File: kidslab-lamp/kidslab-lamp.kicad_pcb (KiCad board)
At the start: 2 copper layers, 129.2 x 177.1 mm, 2 parts, among them U1 Pico

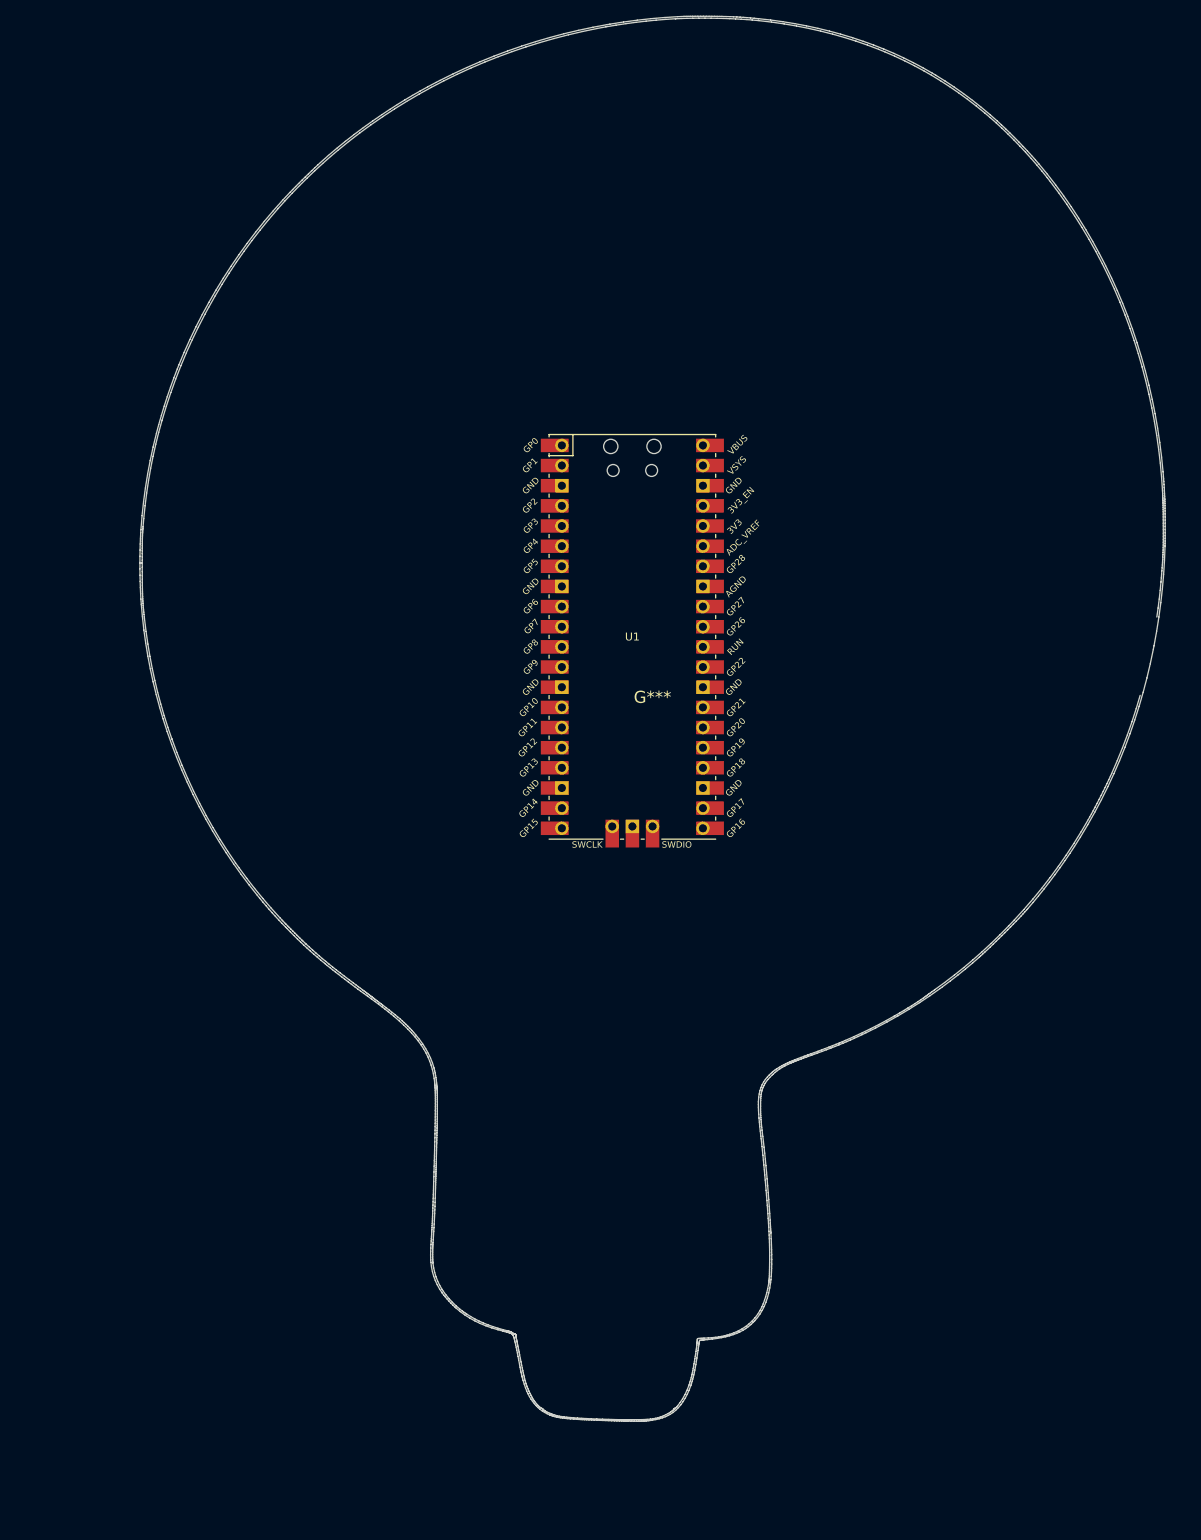
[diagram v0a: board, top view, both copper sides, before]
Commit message: new pcb outline, added frisbee footprints, smaller PCB, added arrow footprints etc.
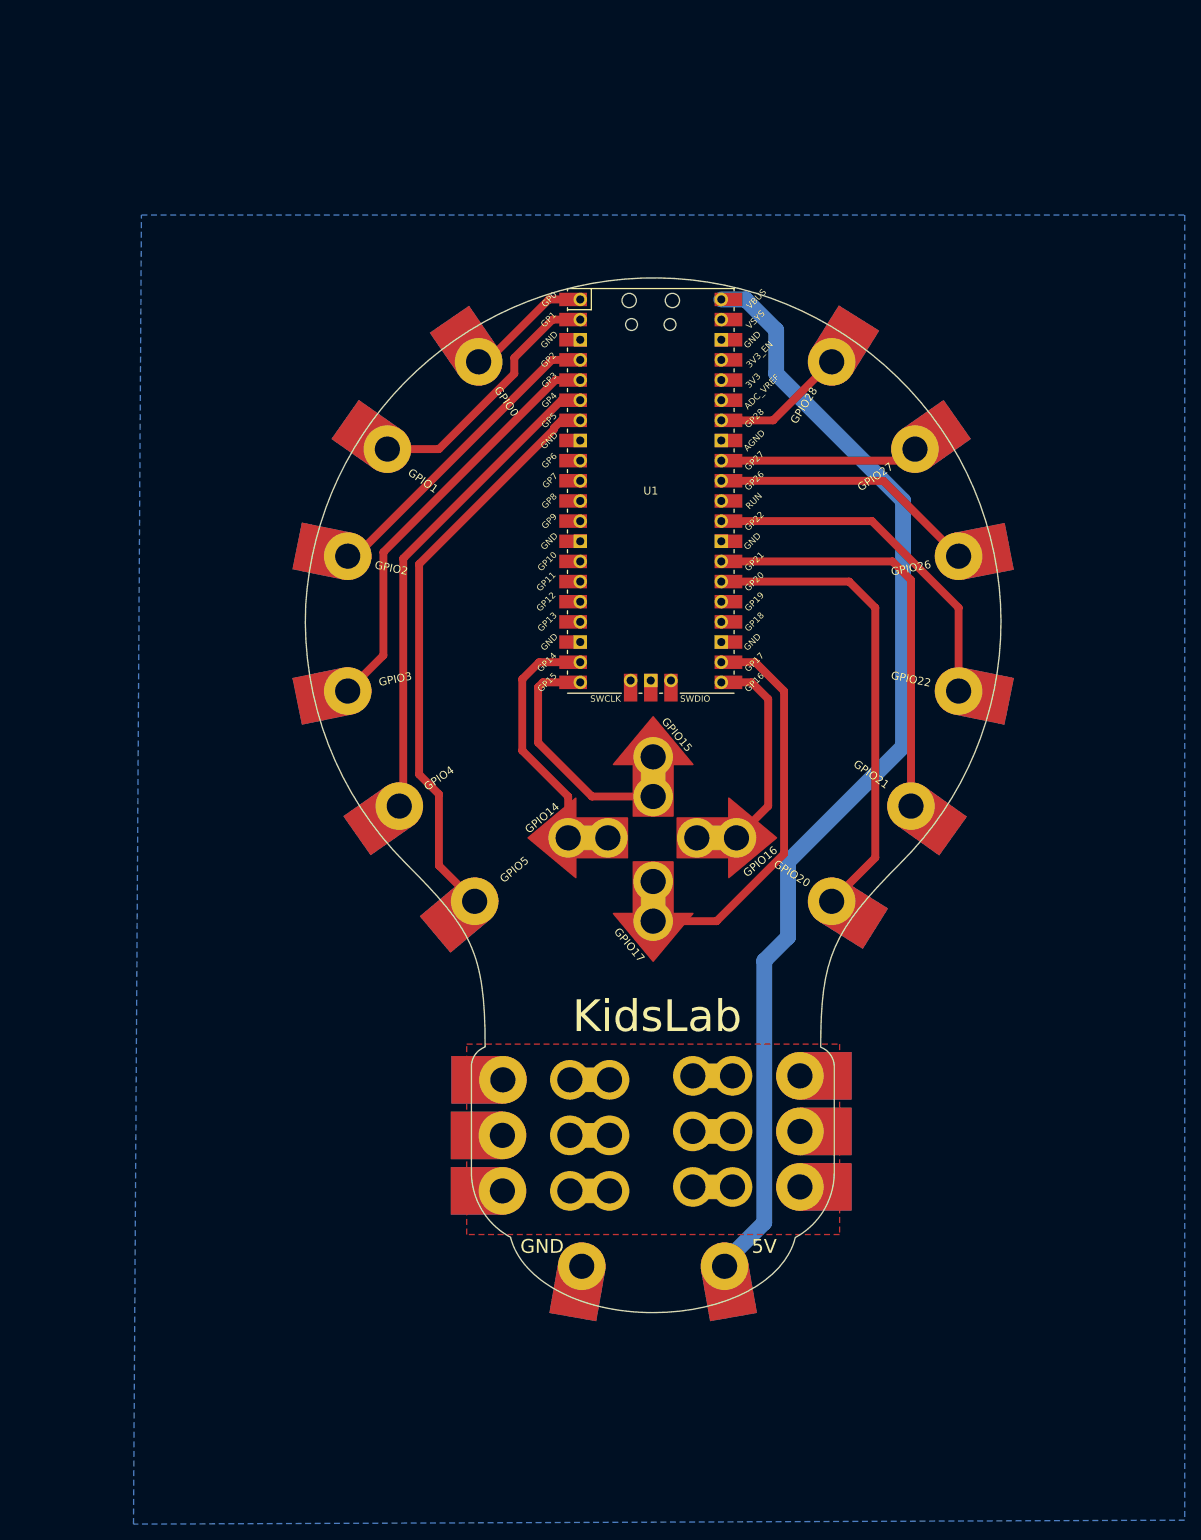
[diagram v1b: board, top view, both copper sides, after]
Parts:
- removed G***: LOGO, lamp-footprint:outline-footprint
- added B1: kroko_board, kidslab:KrokoConnector, F.Cu at (157.4, 153.2)
- added B2: kroko_board, kidslab:KrokoConnector, F.Cu at (141.9, 146.7)
- added B3: kroko_board, kidslab:KrokoConnector, F.Cu at (141.9, 139.7)
- added B4: kroko_board, kidslab:KrokoConnector, F.Cu at (141.9, 153.7)
- added B5: kroko_board, kidslab:KrokoConnector, F.Cu at (157.4, 146.2)
- added B6: kroko_board, kidslab:KrokoConnector, F.Cu at (157.4, 139.2)
- added E30: kroko_edge, kidslab:Edgeconnector, F.Cu at (168.4, 146.2)
- added E31: kroko_edge, kidslab:Edgeconnector, F.Cu at (168.4, 139.2)
- added E32: kroko_edge, kidslab:Edgeconnector, F.Cu at (130.9, 146.7)
- added E33: kroko_edge, kidslab:Edgeconnector, F.Cu at (131.0, 139.7)
- added E34: kroko_edge, kidslab:Edgeconnector, F.Cu at (130.9, 153.7)
- added E35: kroko_edge, kidslab:Edgeconnector, F.Cu at (168.4, 153.2)
- added E36: kroko_edge, kidslab:Edgeconnector, F.Cu at (140.9, 163.2)
- added E37: kroko_edge, kidslab:Edgeconnector, F.Cu at (158.9, 163.2)
- added GPIO0: kroko_edge, kidslab:Edgeconnector, F.Cu at (127.9, 49.2)
- added GPIO1: kroko_edge, kidslab:Edgeconnector, F.Cu at (116.4, 60.2)
- added GPIO14: arrow, kidslab:Kroko_Arrow, F.Cu at (141.7, 109.2)
- added GPIO15: arrow, kidslab:Kroko_Arrow, F.Cu at (149.9, 101.4)
- added GPIO16: arrow, kidslab:Kroko_Arrow, F.Cu at (158.0, 109.2)
- added GPIO17: arrow, kidslab:Kroko_Arrow, F.Cu at (149.9, 117.2)
- added GPIO2: kroko_edge, kidslab:Edgeconnector, F.Cu at (111.4, 73.7)
- added GPIO20: kroko_edge, kidslab:Edgeconnector, F.Cu at (172.4, 117.2)
- added GPIO21: kroko_edge, kidslab:Edgeconnector, F.Cu at (182.4, 105.2)
- added GPIO22: kroko_edge, kidslab:Edgeconnector, F.Cu at (188.4, 90.7)
- added GPIO26: kroko_edge, kidslab:Edgeconnector, F.Cu at (188.4, 73.7)
- added GPIO27: kroko_edge, kidslab:Edgeconnector, F.Cu at (182.9, 60.2)
- added GPIO28: kroko_edge, kidslab:Edgeconnector, F.Cu at (172.4, 49.2)
- added GPIO3: kroko_edge, kidslab:Edgeconnector, F.Cu at (111.4, 90.7)
- added GPIO4: kroko_edge, kidslab:Edgeconnector, F.Cu at (117.9, 105.2)
- added GPIO5: kroko_edge, kidslab:Edgeconnector, F.Cu at (127.4, 117.2)
- added REF**: birne, kidslab:birne, F.Cu at (149.9, 82.3)
- moved U1 18.5 mm to (149.6, 65.4)
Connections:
- U1 pad 1: unconnected-(U1-Pad1) -> Net-(GPIO0-Pad1)
- U1 pad 13: unconnected-(U1-Pad13) -> GND
- U1 pad 18: unconnected-(U1-Pad18) -> GND
- U1 pad 19: unconnected-(U1-Pad19) -> Net-(U1-Pad19)
- U1 pad 2: unconnected-(U1-Pad2) -> Net-(U1-Pad2)
- U1 pad 20: unconnected-(U1-Pad20) -> Net-(U1-Pad20)
- U1 pad 21: unconnected-(U1-Pad21) -> Net-(GPIO16-Pad1)
- U1 pad 22: unconnected-(U1-Pad22) -> Net-(GPIO17-Pad1)
- U1 pad 23: unconnected-(U1-Pad23) -> GND
- U1 pad 26: unconnected-(U1-Pad26) -> Net-(U1-Pad26)
- U1 pad 27: unconnected-(U1-Pad27) -> Net-(U1-Pad27)
- U1 pad 28: unconnected-(U1-Pad28) -> GND
- U1 pad 29: unconnected-(U1-Pad29) -> Net-(U1-Pad29)
- U1 pad 3: unconnected-(U1-Pad3) -> GND
- U1 pad 31: unconnected-(U1-Pad31) -> Net-(U1-Pad31)
- U1 pad 32: unconnected-(U1-Pad32) -> Net-(GPIO27-Pad1)
- U1 pad 34: unconnected-(U1-Pad34) -> Net-(U1-Pad34)
- U1 pad 38: unconnected-(U1-Pad38) -> GND
- U1 pad 4: unconnected-(U1-Pad4) -> Net-(U1-Pad4)
- U1 pad 40: unconnected-(U1-Pad40) -> V_BUS
- U1 pad 5: unconnected-(U1-Pad5) -> Net-(U1-Pad5)
- U1 pad 6: unconnected-(U1-Pad6) -> Net-(U1-Pad6)
- U1 pad 7: unconnected-(U1-Pad7) -> Net-(U1-Pad7)
- U1 pad 8: unconnected-(U1-Pad8) -> GND
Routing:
- net V_BUS: track 0.00 -> 142.7 mm
- net Net-(U1-Pad7): track 0.00 -> 73.3 mm
- net Net-(U1-Pad6): track 0.00 -> 62.0 mm
- net Net-(U1-Pad26): track 0.00 -> 60.1 mm
- net Net-(U1-Pad27): track 0.00 -> 53.4 mm
- net Net-(U1-Pad5): track 0.00 -> 53.2 mm
- net Net-(GPIO17-Pad1): track 0.00 -> 49.9 mm
- net Net-(U1-Pad29): track 0.00 -> 44.9 mm
- net Net-(U1-Pad4): track 0.00 -> 39.6 mm
- net Net-(U1-Pad31): track 0.00 -> 33.8 mm
- net Net-(U1-Pad2): track 0.00 -> 32.2 mm
- net Net-(U1-Pad19): track 0.00 -> 30.6 mm
- net Net-(U1-Pad20): track 0.00 -> 29.9 mm
- net Net-(GPIO16-Pad1): track 0.00 -> 25.9 mm
- net Net-(GPIO27-Pad1): track 0.00 -> 25.0 mm
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- added copper zone on B.Cu, net GND
- added copper zone on F.Cu, net GND
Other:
- board size 129.2 x 177.1 mm -> 87.7 x 130.4 mm
- board text added: "5V"
- board text added: "GND"
- board text added: "KidsLab"

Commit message: added 3.3V rail, replaced GND on bottom with 5V rail added Servo pin header
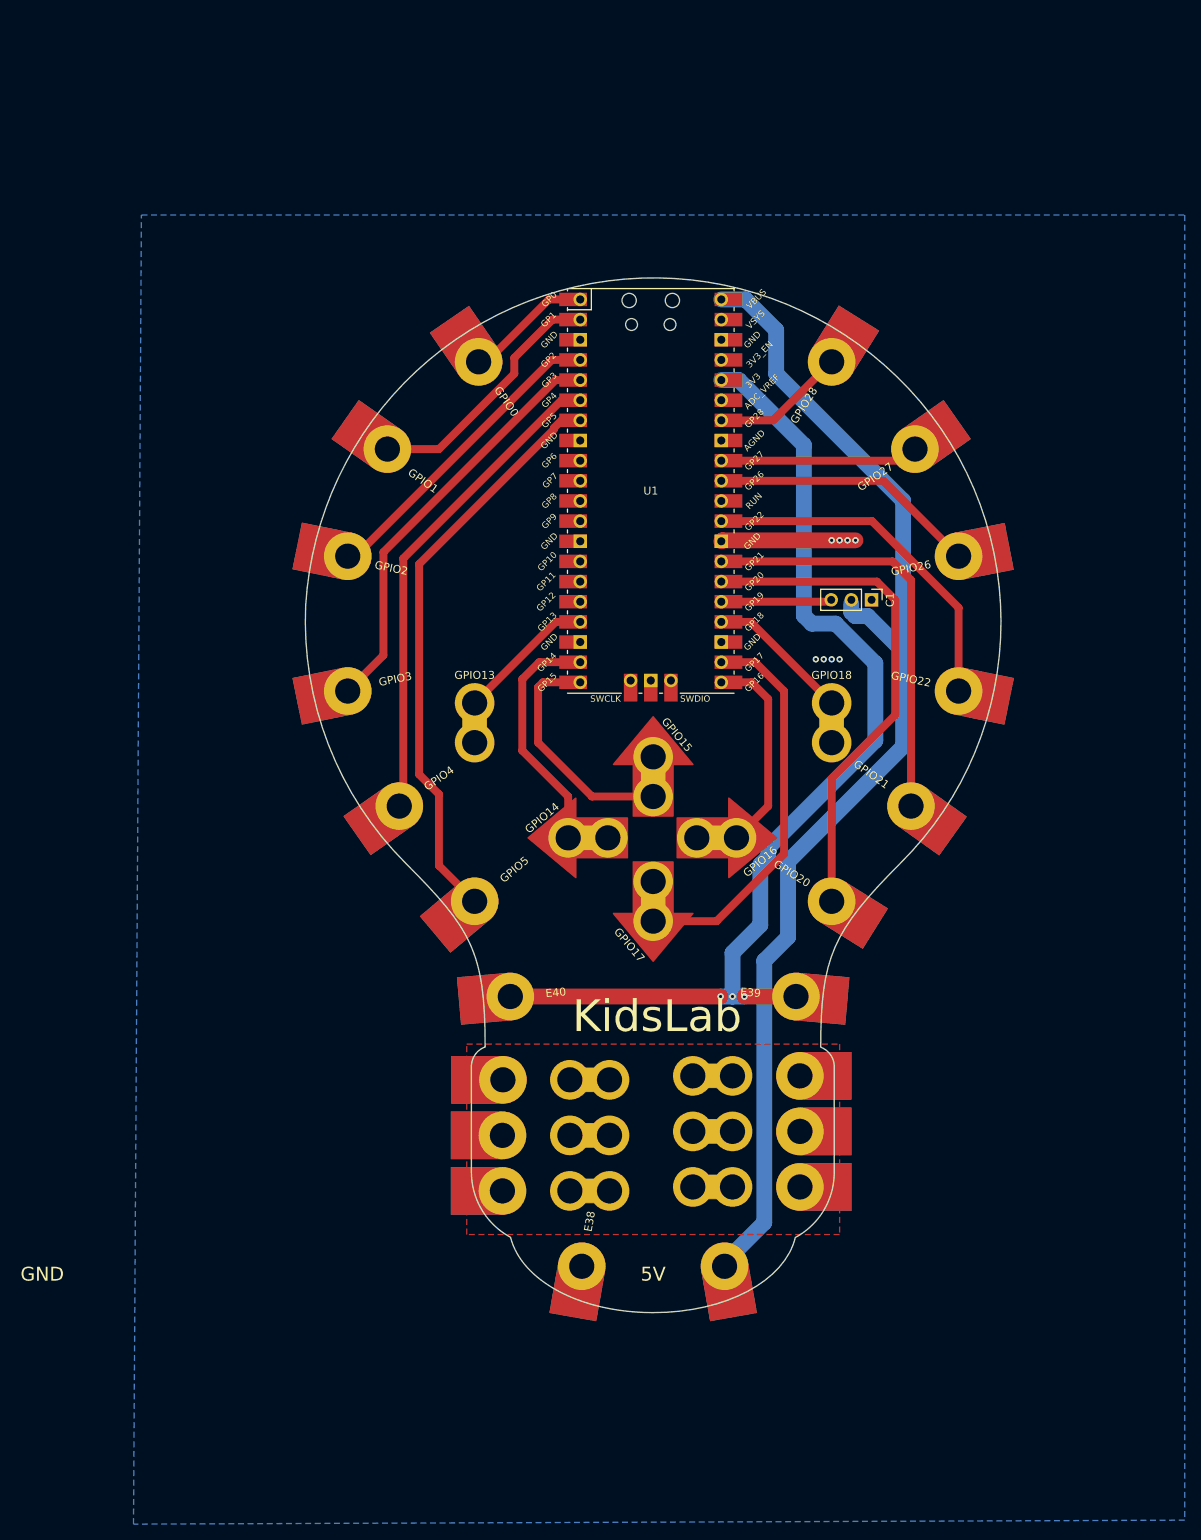
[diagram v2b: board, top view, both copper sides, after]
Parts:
- removed E36: kroko_edge, kidslab:Edgeconnector
- added C1: pin_header_1x3, Connector_PinHeader_2.54mm:PinHeader_1x03_P2.54mm_Vertical, F.Cu at (177.5, 79.2)
- added E38: kroko_edge, kidslab:Edgeconnector, F.Cu at (140.9, 163.2)
- added E39: kroko_edge, kidslab:Edgeconnector, F.Cu at (167.9, 129.2)
- added E40: kroko_edge, kidslab:Edgeconnector, F.Cu at (131.9, 129.2)
- added GPIO13: kroko_board, kidslab:KrokoConnector, F.Cu at (127.4, 94.7)
- added GPIO18: kroko_board, kidslab:KrokoConnector, F.Cu at (172.4, 94.7)
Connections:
- U1 pad 17: unconnected-(U1-Pad17) -> Net-(U1-Pad17)
- U1 pad 24: unconnected-(U1-Pad24) -> Net-(U1-Pad24)
- U1 pad 25: unconnected-(U1-Pad25) -> Net-(U1-Pad25)
- U1 pad 36: unconnected-(U1-Pad36) -> 3.3V
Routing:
- net 3.3V: track 0.00 -> 132.4 mm, vias 0 -> 3
- net Net-(U1-Pad24): track 0.00 -> 18.1 mm
- net Net-(U1-Pad17): track 0.00 -> 17.5 mm
- net GND: track 0.00 -> 17.0 mm, vias 0 -> 8
- net Net-(U1-Pad25): track 0.00 -> 14.0 mm
- net V_BUS: track 142.7 -> 153.8 mm
- net Net-(GPIO20-Pad1): track 60.1 -> 64.2 mm

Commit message: added backside art, LED, and frontside kidslab logo
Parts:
- added D12: SK6812, LED_SMD:LED_SK6812_PLCC4_5.0x5.0mm_P3.2mm, F.Cu at (149.7, 109.2)
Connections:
- U1 pad 16: unconnected-(U1-Pad16) -> Net-(U1-Pad16)
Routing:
- net V_BUS: track 153.8 -> 171.8 mm
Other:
- board text removed: "GND"
- board text removed: "KidsLab"
